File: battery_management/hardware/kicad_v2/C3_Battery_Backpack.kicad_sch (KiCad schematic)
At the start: 17 parts, among them P1 VBUS -> SuperMini 5V, P2 GND -> SuperMini G, P3 CHRG -> GPIO1, P4 VBAT/2 -> GPIO0, P5 VSYS -> W5 A end, P6 BAT+, P7 BAT-, Q1 AO3401 (A19T), U1 TP4054

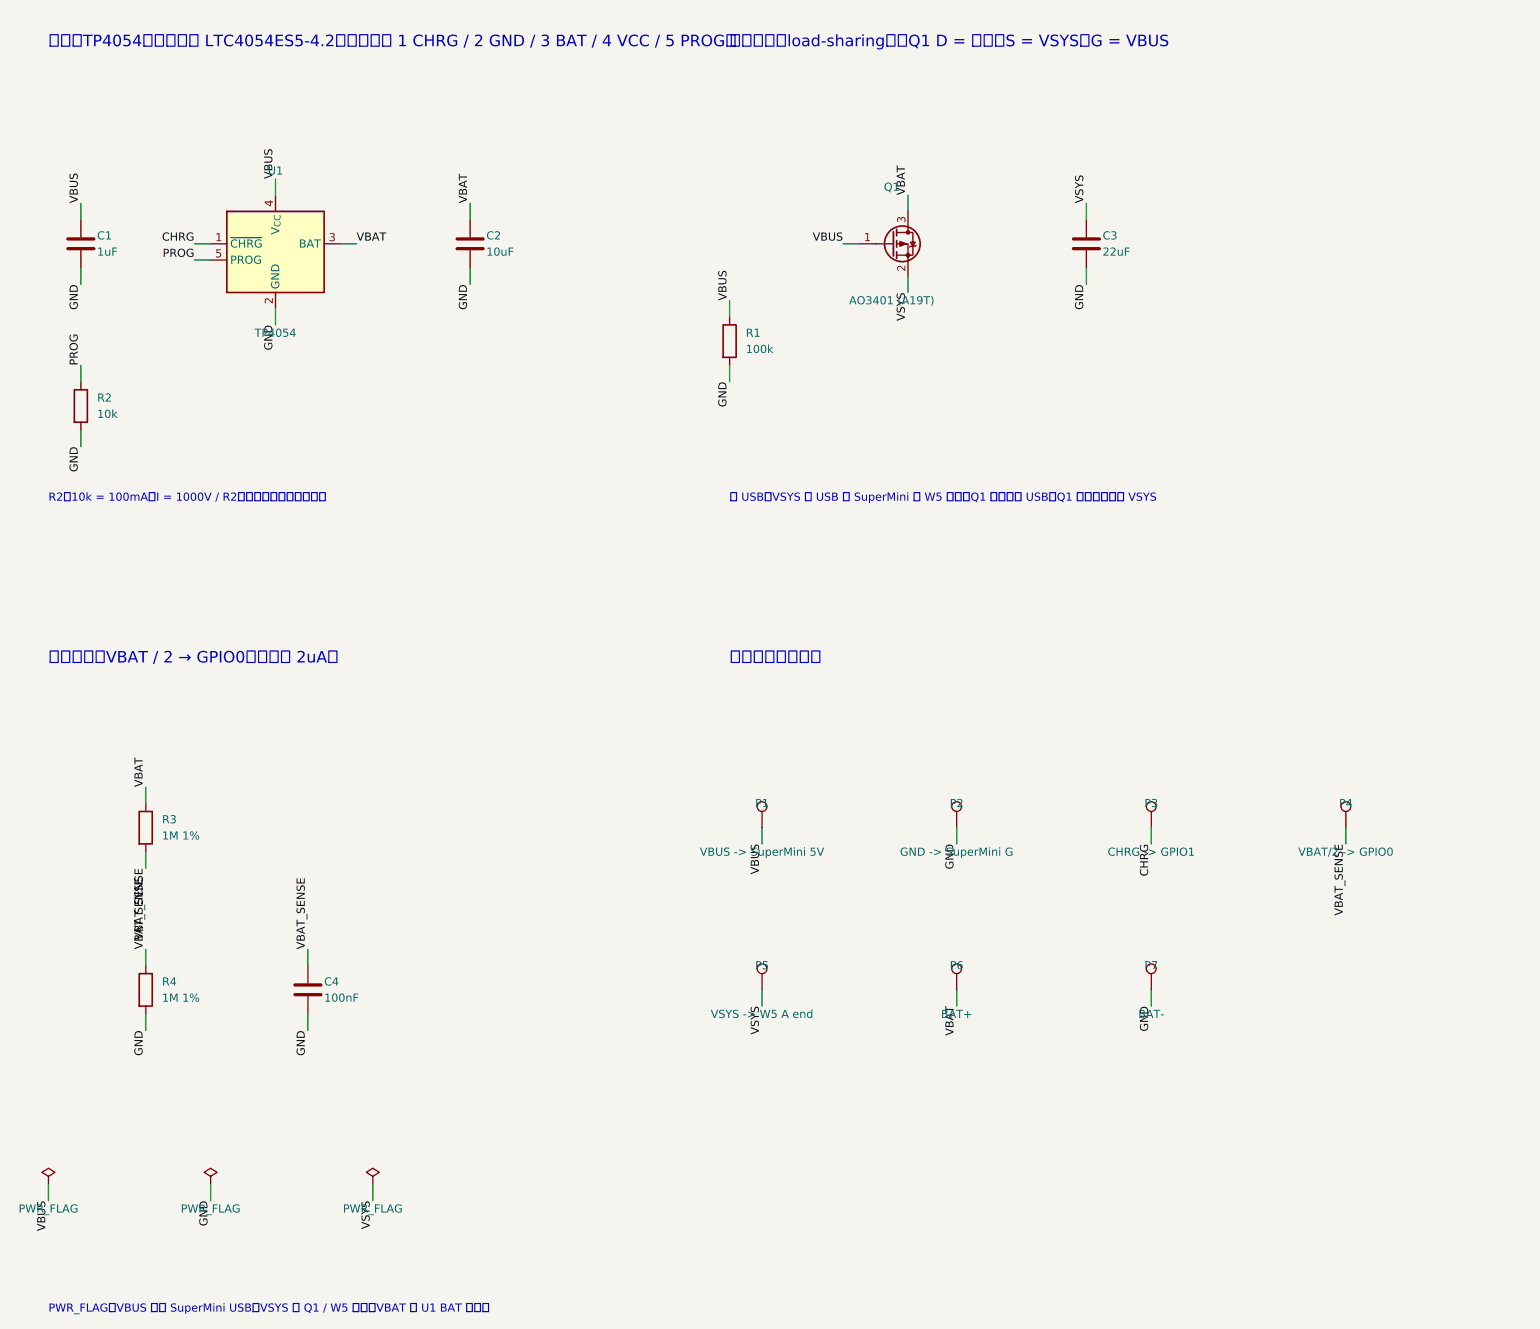
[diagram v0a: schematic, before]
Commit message: 電池背板 v2.1：取消 USB-C 缺口與圓孔，板子縮為 12.0 × 12.8 mm，並輸出電路圖 PDF/PNG/SVG
- 實板 USB-C 固定腳焊點是平的，geom.py 取消 NOTCHES/HOLES，板框改為矩形
- 零件重排為 4 列，5V/G 接點與排針同高；DRC 0 錯誤、0 未連接
- 新 Gerber：C3_Battery_Backpack_v2.1_Gerber.zip（移除 v2.0 zip）
- 新增 gen_outline.py 產生外形與位置圖，更新 PCB_SPEC 與 KiCad README
- gen_sch.py 修正標題重疊、標籤重疊、PWR_FLAG 超出頁面；版本改為 2.1

Co-Authored-By: Claude Opus 5.5 <noreply@anthropic.com>
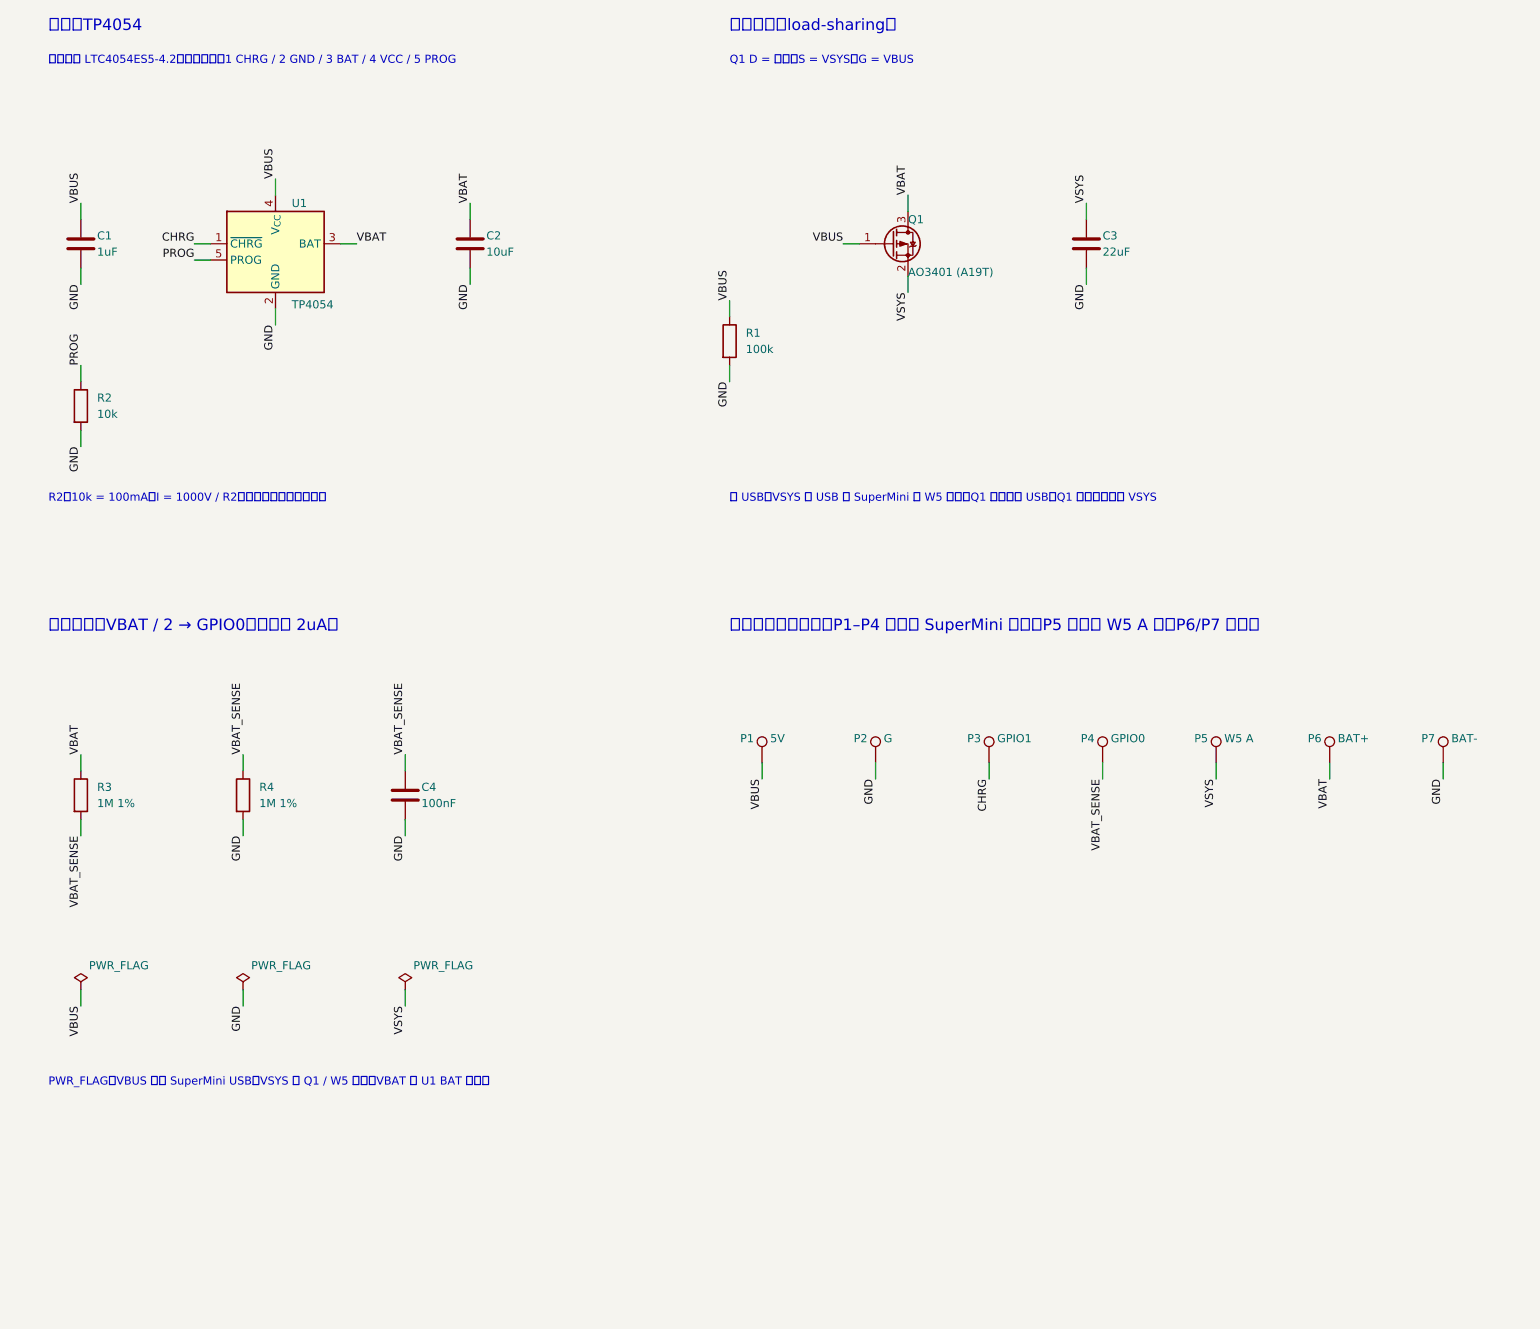
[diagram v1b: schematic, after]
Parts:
- P1: value VBUS -> SuperMini 5V -> 5V
- P2: value GND -> SuperMini G -> G
- P3: value CHRG -> GPIO1 -> GPIO1
- P4: value VBAT/2 -> GPIO0 -> GPIO0
- P5: value VSYS -> W5 A end -> W5 A
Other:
- note added: "Q1 D = 電池、S = VSYS、G = VBUS"
- note added: "充電：TP4054"
- note added: "接點（邊緣焊墊）：P1–P4 跳線到 SuperMini 排針，P5 飛線到 W5 A 端，P6/P7 接電池"
- note added: "符號借用 LTC4054ES5-4.2，腳位相同：1 CHRG / 2 GND / 3 BAT / 4 VCC / 5 PROG"
- note added: "電源路徑（load-sharing）"
- note removed: "充電：TP4054（符號借用 LTC4054ES5-4.2，腳位相同 1 CHRG / 2 GND / 3 BAT / 4 VCC / 5 PROG）"
- note removed: "接點（邊緣焊墊）"
- note removed: "電源路徑（load-sharing）：Q1 D = 電池、S = VSYS、G = VBUS"
- title: ESP32-C3 SuperMini Battery Backpack v2 -> ESP32-C3 SuperMini Battery Backpack v2.1
